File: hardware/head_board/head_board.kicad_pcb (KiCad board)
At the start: 2 copper layers, 90 x 74.7 mm, 130 parts, among them J1 8P8C, J2 CAM, J3 MOTOR, J4 MOTOR, J5 MOTOR, J6 CAMLED, SW1 BOOTSEL, U1 TPS54233, U2 MIC5317-3.3, U3 RP2040, U4 TVS, U5 W25Q128JVS, U6 TMC2209, U7 TMC2209, U8 TMC2209, U9 74HC2G34, Y1 12MHz

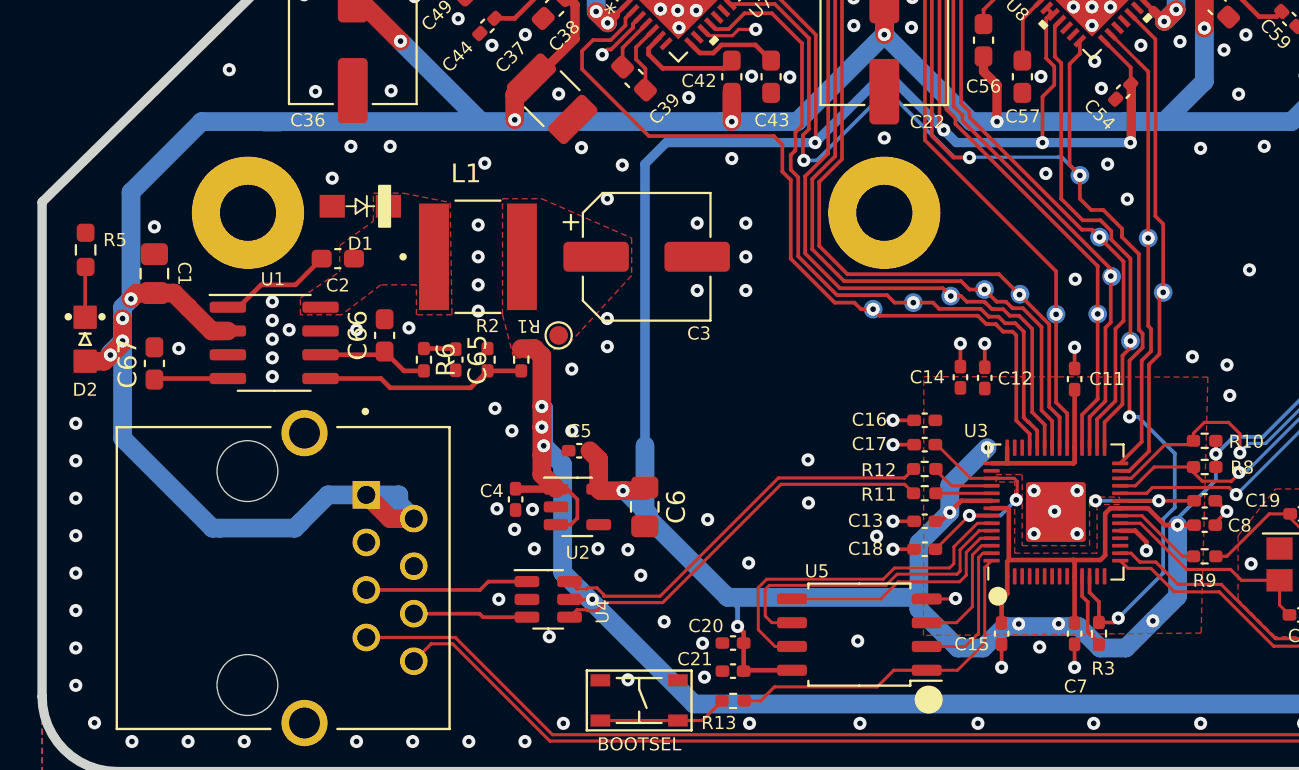
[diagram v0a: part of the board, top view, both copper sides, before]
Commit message: Switch to power module
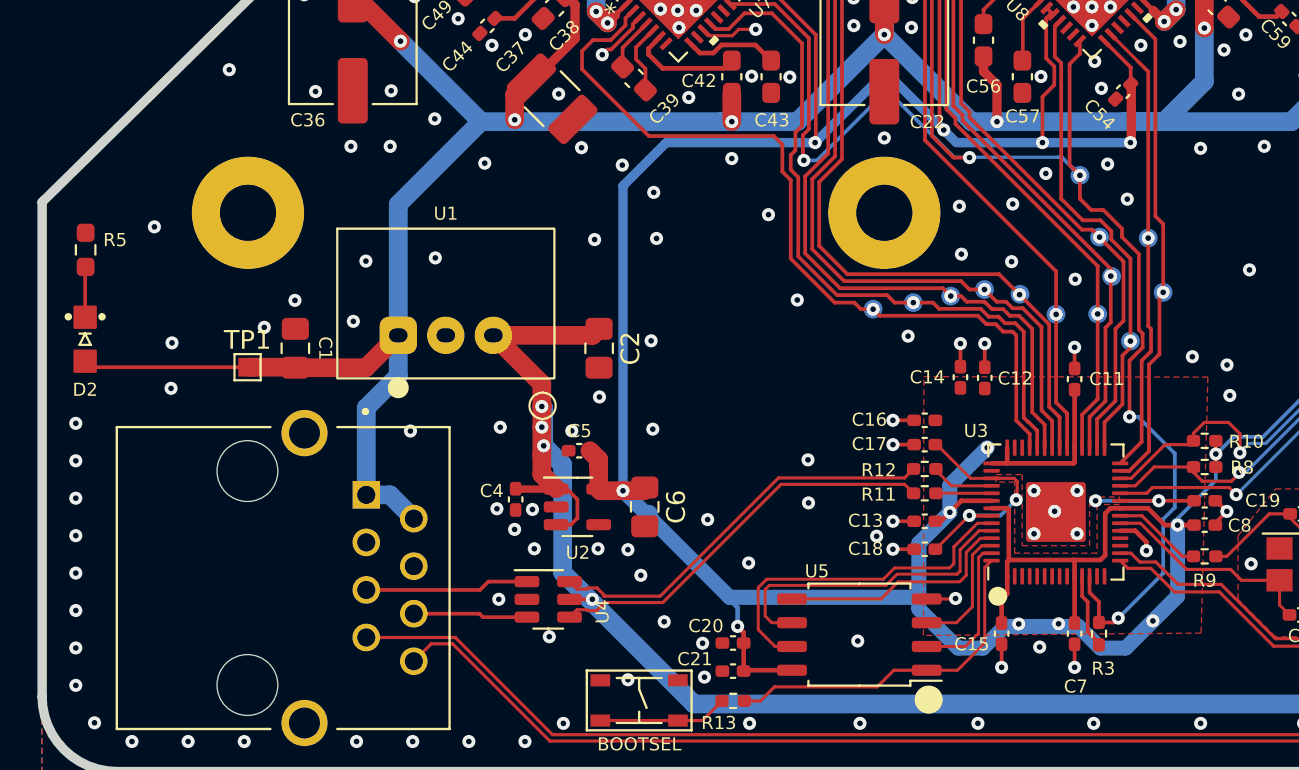
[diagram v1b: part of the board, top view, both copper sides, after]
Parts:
- removed C3: 220u, Capacitor_SMD:CP_Elec_6.3x7.7
- removed C65: 15p, Capacitor_SMD:C_0402_1005Metric_Pad0.74x0.62mm_HandSolder
- removed C66, C67: 22n, Capacitor_SMD:C_0603_1608Metric_Pad1.08x0.95mm_HandSolder
- removed D1: 40V/2A, winterbloom:DIODE_SOD-123_SOD-123F
- removed L1: 22uH, winterbloom:L_Murata_1255AY-220M-P3
- removed R1, R6: 10k, Resistor_SMD:R_0402_1005Metric_Pad0.72x0.64mm_HandSolder
- removed R2: 1.91k, Resistor_SMD:R_0402_1005Metric_Pad0.72x0.64mm_HandSolder
- C2: value 100n -> 22u; footprint Capacitor_SMD:C_0603_1608Metric_Pad1.08x0.95mm_HandSolder -> Capacitor_SMD:C_0805_2012Metric_Pad1.18x1.45mm_HandSolder
- TP1: moved to F.Cu
- U1: value TPS54233 -> P78E05-1000; footprint Package_SO:SOIC-8_3.9x4.9mm_P1.27mm -> winterbloom:Converter_DCDC_CUI_P78E-1000_THT
- moved C2 14.8 mm to (93.0, 120.0), turned to -90 degrees
- moved TP1 13.2 mm to (74.2, 121.0), turned to 0 degrees
- moved C1 8.52 mm to (76.7, 120.0)
- moved U1 6.64 mm to (82.2, 119.3)
- moved TP2 3.86 mm to (89.9, 123.1)
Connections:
- C2 pad 1: /Power/PH -> +5V
- C2 pad 2: /Power/BOOT -> GND
- U1 pad 1: /Power/BOOT -> +24V
- U1 pad 2: +24V -> GND
- U1 pad 3: unconnected-(U1-Pad3) -> +5V
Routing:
- net +24V: track 234.8 -> 211.3 mm, vias 16 -> 12
- net /Power/FB: track 11.3 -> 0.00 mm
- net +5V: track 112.1 -> 118.8 mm
- net /Power/BOOT: track 6.09 -> 0.00 mm
- net /Power/COMP: track 6.03 -> 0.00 mm
- net /Power/SS: track 3.95 -> 0.00 mm
- net Net-(C65-Pad1): track 1.71 -> 0.00 mm
- net +3V3: track 217.3 -> 216.3 mm
- net GND: vias 268 -> 266
- removed copper zone on F.Cu, net +5V
- removed copper zone on F.Cu, net /Power/PH

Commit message: Finish up layout for v1, ended up removing some stuff
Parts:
- removed C1: 22u, Capacitor_SMD:C_0805_2012Metric_Pad1.18x1.45mm_HandSolder
- removed C22: 100u, Capacitor_SMD:CP_Elec_6.3x7.7
- removed the C25 at (103.2, 91.9)
- removed the C26 at (113.2, 93.0)
- removed the C28 at (103.8, 95.2)
- removed the C29 at (108.0, 96.0)
- removed the C36 at (79.8, 103.5)
- removed the C50 at (136.6, 103.5)
- removed the C64 at (140.1, 125.2)
- removed D2: 24V, winterbloom:LED_0805_Kingbright_APT2012
- removed G***: LOGO, winterbloom:Symbol_Winterbloom_40mm
- removed J1: 8P8C, winterbloom:Connector_RJ45_SS-7188S-A-PG4-BA-50
- removed J6: CAMLED, Connector_JST:JST_XH_B3B-XH-AM_1x03_P2.50mm_Vertical
- removed the R5 at (65.5, 114.7)
- removed TP10: M2STP, TestPoint:TestPoint_Pad_D1.0mm
- removed TP11: M2DAG, TestPoint:TestPoint_Pad_D1.0mm
- removed TP12: M2EN, TestPoint:TestPoint_Pad_D1.0mm
- removed TP13: M1DIR, TestPoint:TestPoint_Pad_D1.0mm
- removed TP14: M1STP, TestPoint:TestPoint_Pad_D1.0mm
- removed TP15: M1DAG, TestPoint:TestPoint_Pad_D1.0mm
- removed TP16: M1EN, TestPoint:TestPoint_Pad_D1.0mm
- removed TP18: M0STP, TestPoint:TestPoint_Pad_D1.0mm
- removed TP19: M0DAG, TestPoint:TestPoint_Pad_D1.0mm
- removed TP20: M0EN, TestPoint:TestPoint_Pad_D1.0mm
- removed TP21: UART, TestPoint:TestPoint_Pad_D1.0mm
- removed TP22: AUX, TestPoint:TestPoint_Pad_D1.0mm
- removed the U4 at (90.2, 133.4)
- removed the U9 at (140.1, 122.5)
- added C10: 10u, Capacitor_SMD:C_0805_2012Metric_Pad1.18x1.45mm_HandSolder, F.Cu at (121.0, 85.0)
- added C27: 100n, Capacitor_SMD:C_0402_1005Metric_Pad0.74x0.62mm_HandSolder, F.Cu at (114.5, 90.2)
- added C3: 22u, Capacitor_SMD:C_0805_2012Metric_Pad1.18x1.45mm_HandSolder, F.Cu at (82.8, 83.8)
- added C42: 22n, Capacitor_SMD:C_0603_1608Metric_Pad1.08x0.95mm_HandSolder, F.Cu at (99.8, 67.9)
- added C43: 100n, Capacitor_SMD:C_0402_1005Metric_Pad0.74x0.62mm_HandSolder, F.Cu at (112.0, 69.1)
- added C44: 100n, Capacitor_SMD:C_0603_1608Metric_Pad1.08x0.95mm_HandSolder, F.Cu at (97.5, 68.9)
- added C45: 4.7u, Capacitor_SMD:C_0603_1608Metric_Pad1.08x0.95mm_HandSolder, F.Cu at (99.8, 72.0)
- added C7: 1u, Capacitor_SMD:C_0402_1005Metric_Pad0.74x0.62mm_HandSolder, F.Cu at (117.8, 85.0)
- added C8: 100n, Capacitor_SMD:C_0402_1005Metric_Pad0.74x0.62mm_HandSolder, F.Cu at (76.5, 77.2)
- added C9: 100n, Capacitor_SMD:C_0402_1005Metric_Pad0.74x0.62mm_HandSolder, F.Cu at (80.5, 77.2)
- added D4: ACT, winterbloom:LED_0805_Kingbright_APT2012, F.Cu at (142.2, 89.5)
- added FB1: 50Ω @ 100MHz, Inductor_SMD:L_0603_1608Metric_Pad1.05x0.95mm_HandSolder, F.Cu at (78.5, 77.8)
- added FB10: 50Ω @ 100MHz, Inductor_SMD:L_0603_1608Metric_Pad1.05x0.95mm_HandSolder, F.Cu at (81.7, 67.6)
- added FB11: 50Ω @ 100MHz, Inductor_SMD:L_0603_1608Metric_Pad1.05x0.95mm_HandSolder, F.Cu at (88.7, 67.1)
- added FB12: 50Ω @ 100MHz, Inductor_SMD:L_0603_1608Metric_Pad1.05x0.95mm_HandSolder, F.Cu at (90.7, 65.1)
- added FB13: 50Ω @ 100MHz, Inductor_SMD:L_0603_1608Metric_Pad1.05x0.95mm_HandSolder, F.Cu at (91.5, 57.6)
- added FB14: 50Ω @ 100MHz, Inductor_SMD:L_0603_1608Metric_Pad1.05x0.95mm_HandSolder, F.Cu at (79.5, 82.2)
- added FB2: 50Ω @ 100MHz, Inductor_SMD:L_0603_1608Metric_Pad1.05x0.95mm_HandSolder, F.Cu at (118.8, 57.6)
- added FB3: 50Ω @ 100MHz, Inductor_SMD:L_0603_1608Metric_Pad1.05x0.95mm_HandSolder, F.Cu at (118.8, 64.0)
- added FB4: 50Ω @ 100MHz, Inductor_SMD:L_0603_1608Metric_Pad1.05x0.95mm_HandSolder, F.Cu at (120.8, 65.8)
- added FB5: 50Ω @ 100MHz, Inductor_SMD:L_0603_1608Metric_Pad1.05x0.95mm_HandSolder, F.Cu at (128.0, 67.2)
- added FB6: 50Ω @ 100MHz, Inductor_SMD:L_0603_1608Metric_Pad1.05x0.95mm_HandSolder, F.Cu at (99.5, 53.4)
- added FB7: 50Ω @ 100MHz, Inductor_SMD:L_0603_1608Metric_Pad1.05x0.95mm_HandSolder, F.Cu at (104.5, 57.9)
- added FB8: 50Ω @ 100MHz, Inductor_SMD:L_0603_1608Metric_Pad1.05x0.95mm_HandSolder, F.Cu at (106.5, 57.9)
- added FB9: 50Ω @ 100MHz, Inductor_SMD:L_0603_1608Metric_Pad1.05x0.95mm_HandSolder, F.Cu at (111.5, 53.4)
- added J3: CAM, Connector_JST:JST_XH_B4B-XH-AM_1x04_P2.50mm_Vertical, F.Cu at (95.2, 101.6)
- added J4: CAMLED, Connector_JST:JST_XH_B3B-XH-AM_1x03_P2.50mm_Vertical, F.Cu at (106.5, 101.6)
- added J5: AUX, Connector_JST:JST_XH_B3B-XH-AM_1x03_P2.50mm_Vertical, F.Cu at (117.8, 101.6)
- added R10: 1k, Resistor_SMD:R_0603_1608Metric_Pad0.98x0.95mm_HandSolder, F.Cu at (142.2, 85.0)
- added R12: 10k, Resistor_SMD:R_0402_1005Metric_Pad0.72x0.64mm_HandSolder, F.Cu at (134.2, 102.6)
- added R13: 10k, Resistor_SMD:R_0402_1005Metric_Pad0.72x0.64mm_HandSolder, F.Cu at (112.0, 93.8)
- added R14: 10k, Resistor_SMD:R_0402_1005Metric_Pad0.72x0.64mm_HandSolder, F.Cu at (117.8, 93.8)
- added R17: 10k, Resistor_SMD:R_0402_1005Metric_Pad0.72x0.64mm_HandSolder, F.Cu at (131.9, 81.4)
- added R20: 10k, Resistor_SMD:R_0402_1005Metric_Pad0.72x0.64mm_HandSolder, F.Cu at (103.1, 74.0)
- added R23: 10k, Resistor_SMD:R_0402_1005Metric_Pad0.72x0.64mm_HandSolder, F.Cu at (124.0, 84.8)
- added RV1: 35V, Resistor_SMD:R_0603_1608Metric_Pad0.98x0.95mm_HandSolder, F.Cu at (76.8, 82.2)
- added RV2: 35V, Resistor_SMD:R_0603_1608Metric_Pad0.98x0.95mm_HandSolder, F.Cu at (122.7, 60.0)
- added RV3: 35V, Resistor_SMD:R_0603_1608Metric_Pad0.98x0.95mm_HandSolder, F.Cu at (126.2, 63.5)
- added RV4: 35V, Resistor_SMD:R_0603_1608Metric_Pad0.98x0.95mm_HandSolder, F.Cu at (103.0, 52.4)
- added RV5: 35V, Resistor_SMD:R_0603_1608Metric_Pad0.98x0.95mm_HandSolder, F.Cu at (108.0, 52.4)
- added RV6: 35V, Resistor_SMD:R_0603_1608Metric_Pad0.98x0.95mm_HandSolder, F.Cu at (83.9, 63.5)
- added RV7: 35V, Resistor_SMD:R_0603_1608Metric_Pad0.98x0.95mm_HandSolder, F.Cu at (87.4, 60.0)
- added U5: TVS, Package_TO_SOT_SMD:SOT-23-6, F.Cu at (85.5, 95.5)
- added U6: TVS, Package_TO_SOT_SMD:SOT-23-6, F.Cu at (85.4, 90.5)
- added U7: 74HC2G34, Package_TO_SOT_SMD:SOT-363_SC-70-6, F.Cu at (115.0, 93.0)
- C2: value 22u -> 4.7u
- C4: value 1u -> 22u; footprint Capacitor_SMD:C_0402_1005Metric_Pad0.74x0.62mm_HandSolder -> Capacitor_SMD:C_0805_2012Metric_Pad1.18x1.45mm_HandSolder
- C5: value 1u -> 100u; footprint Capacitor_SMD:C_0402_1005Metric_Pad0.74x0.62mm_HandSolder -> Capacitor_SMD:CP_Elec_6.3x7.7
- C6: value 10u -> 1u; footprint Capacitor_SMD:C_0805_2012Metric_Pad1.18x1.45mm_HandSolder -> Capacitor_SMD:C_0402_1005Metric_Pad0.74x0.62mm_HandSolder
- J2: value CAM -> 8P8C; footprint Connector_JST:JST_XH_B4B-XH-AM_1x04_P2.50mm_Vertical -> winterbloom:Connector_RJ45_ASSMANN_A-2014-2S-4-N-R
- J7: renamed from J4; moved to B.Cu
- J8: renamed from J3; moved to B.Cu
- J9: renamed from J5; moved to B.Cu
- R11: renamed from R9; value 1K -> 1k
- R18: renamed from R4; value 22R -> 220m
- R19: renamed from R17; value 22R -> 220m
- R21: renamed from R14; value 22R -> 220m
- R22: renamed from R16; value 22R -> 220m
- R24: renamed from R18; value 22R -> 220m
- R25: renamed from R20; value 22R -> 220m
- R4: renamed from R10; value 10K -> 10k
- R5: renamed from R8; value 10K -> 10k
- R8: renamed from R3; value 1K -> 1k
- R9: renamed from R13; value 1K -> 1k
- TP1: value 24V -> GND; moved to B.Cu
- TP17: value M0DIR -> UART
- TP2: value 5V -> 24V; footprint TestPoint:TestPoint_Pad_D1.0mm -> TestPoint:TestPoint_Pad_1.0x1.0mm; moved to B.Cu
- TP3: value 3V3 -> 5V
- TP5: value RST -> GND
- TP6: value SWD -> 3V3
- TP7: value SWCLK -> ~{RST}
- TP8: value GND -> SWD
- TP9: value M2DIR -> SWC
- U1: value P78E05-1000 -> VX7805-500; footprint winterbloom:Converter_DCDC_CUI_P78E-1000_THT -> winterbloom:Converter_DCDC_CUI_VX78-500_THT
- moved J2 81.9 mm to (76.2, 94.6)
- moved H3 65.2 mm to (105.2, 47.6)
- moved SW1 58.9 mm to (140.5, 101.3), turned to 0 degrees
- moved C67 57.1 mm to (93.5, 57.6), turned to -90 degrees
- moved C35 54.0 mm to (133.5, 74.0), turned to 90 degrees
- moved C69 53.6 mm to (92.7, 63.6), turned to -90 degrees
- moved C40 53.3 mm to (116.8, 57.6), turned to -90 degrees
- moved R8 52.6 mm to (136.0, 85.2), turned to -90 degrees
- moved R9 51.8 mm to (136.4, 101.9), turned to -90 degrees
- moved C61 51.1 mm to (92.7, 67.2), turned to 90 degrees
- moved C4 50.4 mm to (109.9, 82.5), turned to 90 degrees
- moved C25 49.8 mm to (134.2, 101.0), turned to 0 degrees
- moved C26 49.8 mm to (134.2, 99.5), turned to 0 degrees
- moved C38 49.8 mm to (116.8, 61.8), turned to -90 degrees
- moved U2 49.0 mm to (114.5, 85.0)
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- renumbered C7 to C11, C8 to C12, C11 to C13, C12 to C14, C13 to C15, C14 to C16, C15 to C17, C16 to C18, C17 to C19, C18 to C20, C19 to C21, C9 to C23, C10 to C24, C21 to C25, C20 to C26, C39 to C28, C40 to C29, C42 to C30, C43 to C31, C44 to C32, C45 to C33, C37 to C35, C38 to C36, C41 to C37, C48 to C38, C46 to C39, C49 to C40, C47 to C41, C30 to C46, C31 to C47, C23 to C49, C24 to C50, C27 to C51, C34 to C52, C32 to C53, C35 to C54, C33 to C55, C53 to C56, C54 to C57, C56 to C58, C57 to C59, C58 to C60, C59 to C61, C51 to C63, C52 to C64, C55 to C65, C62 to C66, C60 to C67, C63 to C68, C61 to C69, R11 to R6, R12 to R7, U8 to U10, U5 to U4, U7 to U8, U6 to U9
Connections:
- net /MCU/QSPI_CS renamed /Microcontroller/QSPI_CS
- net /MCU/QSPI_SCLK renamed /Microcontroller/QSPI_SCLK
- net /MCU/QSPI_SD0 renamed /Microcontroller/QSPI_SD0
- net /MCU/QSPI_SD1 renamed /Microcontroller/QSPI_SD1
- net /MCU/QSPI_SD2 renamed /Microcontroller/QSPI_SD2
- net /MCU/QSPI_SD3 renamed /Microcontroller/QSPI_SD3
- net /MCU/XOUT renamed /Microcontroller/XOUT
- C2 pad 1: +5V -> Net-(C2-Pad1)
- C23 pad 1: /MCU/XIN -> /Microcontroller/XIN
- C24 pad 1: Net-(C10-Pad1) -> Net-(C24-Pad1)
- C30 pad 1: +24V -> VMOTOR
- C35 pad 1: +24V -> VMOTOR
- C36 pad 1: +24V -> VMOTOR
- C37 pad 1: +24V -> VMOTOR
- C38 pad 1: Net-(C48-Pad1) -> Net-(C38-Pad1)
- C39 pad 1: Net-(C46-Pad1) (its old number) -> Net-(C39-Pad1)
- C40 pad 1: Net-(C49-Pad1) -> Net-(C40-Pad1)
- C41 pad 1: Net-(C47-Pad1) (its old number) -> Net-(C41-Pad1)
- C49 pad 1: +24V -> VMOTOR
- C5 pad 1: +3V3 -> VMOTOR
- C50 pad 1: +24V -> VMOTOR
- C51 pad 1: +24V -> VMOTOR
- C52 pad 1: Net-(C34-Pad1) -> Net-(C52-Pad1)
- C53 pad 1: Net-(C32-Pad1) (its old number) -> Net-(C53-Pad1)
- C54 pad 1: Net-(C35-Pad1) -> Net-(C54-Pad1)
- C55 pad 1: Net-(C33-Pad1) (its old number) -> Net-(C55-Pad1)
- C58 pad 1: +24V -> VMOTOR
- C6 pad 1: +3V3 -> +5V
- C63 pad 1: +24V -> VMOTOR
- C64 pad 1: +24V -> VMOTOR
- C65 pad 1: +24V -> VMOTOR
- C66 pad 1: Net-(C62-Pad1) -> Net-(C66-Pad1)
- C67 pad 1: Net-(C60-Pad1) (its old number) -> Net-(C67-Pad1)
- C68 pad 1: Net-(C63-Pad1) -> Net-(C68-Pad1)
- C69 pad 1: Net-(C61-Pad1) (its old number) -> Net-(C69-Pad1)
- J2 pad 1: +5V -> +24V
- J2 pad 2: /Connections/CAM_D- -> +24V
- J2 pad 3: /Connections/CAM_D+ -> GND
- J7 pad 1: Net-(C49-Pad1) -> Net-(C39-Pad1)
- J7 pad 2: Net-(C48-Pad1) -> Net-(C41-Pad1)
- J7 pad 3: Net-(C47-Pad1) (its old number) -> Net-(C38-Pad1)
- J7 pad 4: Net-(C46-Pad1) (its old number) -> Net-(C40-Pad1)
- J8 pad 1: Net-(C35-Pad1) -> Net-(C53-Pad1)
- J8 pad 2: Net-(C34-Pad1) -> Net-(C55-Pad1)
- J8 pad 3: Net-(C33-Pad1) (its old number) -> Net-(C52-Pad1)
- J8 pad 4: Net-(C32-Pad1) (its old number) -> Net-(C54-Pad1)
- J9 pad 1: Net-(C63-Pad1) -> Net-(C67-Pad1)
- J9 pad 2: Net-(C62-Pad1) -> Net-(C69-Pad1)
- J9 pad 3: Net-(C61-Pad1) (its old number) -> Net-(C66-Pad1)
- J9 pad 4: Net-(C60-Pad1) (its old number) -> Net-(C68-Pad1)
- R11 pad 2: Net-(C10-Pad1) -> Net-(C24-Pad1)
- R4 pad 1: /MCU/RUN -> /Microcontroller/RUN
- R5 pad 2: /MCU/SWD -> /Microcontroller/SWD
- R6 pad 1: /MCU/USB_D+ -> /Microcontroller/USB_D+
- R7 pad 1: /MCU/USB_D- -> /Microcontroller/USB_D-
- R8 pad 1: /MCU/UART1_TX -> /Microcontroller/UART1_TX
- TP1 pad 1: +24V -> GND
- TP17 pad 1: /Left Motor/DIR -> /TMC_UART
- TP2 pad 1: +5V -> +24V
- TP3 pad 1: +3V3 -> +5V
- TP5 pad 1: /MCU/RUN -> GND
- TP6 pad 1: /MCU/SWD -> +3V3
- TP7 pad 1: /MCU/SWCLK -> /Microcontroller/RUN
- TP8 pad 1: GND -> /Microcontroller/SWD
- TP9 pad 1: /MCU/M2_DIR -> /Microcontroller/SWCLK
- U1 pad 1: +24V -> Net-(C2-Pad1)
- U10 pad 1: Net-(C63-Pad1) -> /Right Motor/OB2
- U10 pad 11: /MCU/M2_DIAG -> /Microcontroller/M2_DIAG
- U10 pad 16: /MCU/M2_STEP -> /Microcontroller/M2_STEP
- U10 pad 19: /MCU/M2_DIR -> /Microcontroller/M2_DIR
- U10 pad 2: /MCU/M2_EN -> /Microcontroller/M2_EN
- U10 pad 21: Net-(C60-Pad1) (its old number) -> /Right Motor/OA2
- U10 pad 22: +24V -> VMOTOR
- U10 pad 24: Net-(C61-Pad1) (its old number) -> /Right Motor/OA1
- U10 pad 26: Net-(C62-Pad1) -> /Right Motor/OB1
- U10 pad 28: +24V -> VMOTOR
- U3 pad 11: /MCU/UART1_TX -> unconnected-(U3-Pad11)
- U3 pad 12: /TMC_UART -> unconnected-(U3-Pad12)
- U3 pad 15: /MCU/CAM_LED_LV -> unconnected-(U3-Pad15)
- U3 pad 16: /MCU/AUX_LV -> unconnected-(U3-Pad16)
- U3 pad 18: unconnected-(U3-Pad18) -> /Microcontroller/ACT_LED
- U3 pad 2: unconnected-(U3-Pad2) -> /Connections/CAM_LED
- U3 pad 20: /MCU/XIN -> /Microcontroller/XIN
- U3 pad 24: /MCU/SWCLK -> /Microcontroller/SWCLK
- U3 pad 25: /MCU/SWD -> /Microcontroller/SWD
- U3 pad 26: /MCU/RUN -> /Microcontroller/RUN
- U3 pad 27: /MCU/M2_DIR -> /Microcontroller/UART1_TX
- U3 pad 28: /MCU/M2_STEP -> /TMC_UART
- U3 pad 29: /MCU/M2_DIAG -> /Left Motor/DIR
- U3 pad 3: unconnected-(U3-Pad3) -> /Connections/AUX_OUT
- U3 pad 30: /MCU/M2_EN -> /Left Motor/STEP
- U3 pad 31: /MCU/M1_DIR -> /Left Motor/DIAG
- U3 pad 32: /MCU/M1_STEP -> /Left Motor/ENN
- U3 pad 34: /MCU/M1_DIAG -> /Microcontroller/M1_DIR
- U3 pad 35: /MCU/M1_EN -> /Microcontroller/M1_STEP
- U3 pad 36: /Left Motor/DIR -> /Microcontroller/M1_DIAG
- U3 pad 37: /Left Motor/STEP -> /Microcontroller/M1_EN
- U3 pad 38: /Left Motor/DIAG -> /Microcontroller/M2_DIR
- U3 pad 39: /Left Motor/ENN -> /Microcontroller/M2_STEP
- U3 pad 40: unconnected-(U3-Pad40) -> /Microcontroller/M2_DIAG
- U3 pad 41: unconnected-(U3-Pad41) -> /Microcontroller/M2_EN
- U8 pad 1: Net-(C49-Pad1) -> /Left Motor/OB2
- U8 pad 21: Net-(C46-Pad1) (its old number) -> /Left Motor/OA2
- U8 pad 22: +24V -> VMOTOR
- U8 pad 24: Net-(C47-Pad1) (its old number) -> /Left Motor/OA1
- U8 pad 26: Net-(C48-Pad1) -> /Left Motor/OB1
- U8 pad 28: +24V -> VMOTOR
- U9 pad 1: Net-(C35-Pad1) -> /Z Motor/OB2
- U9 pad 11: /MCU/M1_DIAG -> /Microcontroller/M1_DIAG
- U9 pad 16: /MCU/M1_STEP -> /Microcontroller/M1_STEP
- U9 pad 19: /MCU/M1_DIR -> /Microcontroller/M1_DIR
- U9 pad 2: /MCU/M1_EN -> /Microcontroller/M1_EN
- U9 pad 21: Net-(C32-Pad1) (its old number) -> /Z Motor/OA2
- U9 pad 22: +24V -> VMOTOR
- U9 pad 24: Net-(C33-Pad1) (its old number) -> /Z Motor/OA1
- U9 pad 26: Net-(C34-Pad1) -> /Z Motor/OB1
- U9 pad 28: +24V -> VMOTOR
- Y1 pad 1: Net-(C10-Pad1) -> /Microcontroller/XIN
- Y1 pad 3: /MCU/XIN -> Net-(C24-Pad1)
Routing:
- net +24V: track 211.3 -> 20.8 mm, vias 12 -> 1
- net GND: track 27.8 -> 168.6 mm, vias 266 -> 84
- net VMOTOR: track 0.00 -> 137.4 mm, vias 0 -> 10
- net /Microcontroller/USB_D-: track 0.00 -> 70.7 mm
- net /Microcontroller/USB_D+: track 0.00 -> 70.1 mm
- net /Microcontroller/M2_EN: track 0.00 -> 56.4 mm, vias 0 -> 2
- net /MCU/M1_EN: track 53.1 -> 0.00 mm, vias 1 -> 0
- net +5V: track 118.8 -> 71.0 mm, vias 4 -> 2
- net /Microcontroller/M2_DIAG: track 0.00 -> 47.0 mm
- net /Microcontroller/M2_DIR: track 0.00 -> 46.1 mm
- net /Microcontroller/M1_EN: track 0.00 -> 45.7 mm, vias 0 -> 2
- net /Microcontroller/M2_STEP: track 0.00 -> 45.4 mm
- net /Connections/CAM_D-: track 73.8 -> 29.0 mm
- net /MCU/M1_DIR: track 43.6 -> 0.00 mm, vias 1 -> 0
- net /Connections/CAM_D+: track 71.6 -> 28.8 mm
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- added copper zone on F.Cu, net +24V
- added copper zone on In2.Cu, net +3V3
- added copper zone on F.Cu, net +5V
- added copper zone on In1.Cu, net GND
- added copper zone on F.Cu, net VMOTOR
- added copper zone on In2.Cu, net VMOTOR
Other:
- board size 90 x 74.7 mm -> 80 x 64.4 mm
- copper layers 2 -> 4
- board text added: "${TITLE} ${REVISION} ${ISSUE_DATE} ${COMPANY} ${COMMENT3} ${COMMENT2} ${COMMENT1}"
- board text added: "AUX"
- board text removed: "${TITLE} ${REVISION} ${ISSUE_DATE} ${COMMENT1} ${COMMENT2} ${COMMENT3}"
- board text removed: "L"
- board text removed: "R"
- board text removed: "TRANS RIGHTS"
- board text removed: "Z"
